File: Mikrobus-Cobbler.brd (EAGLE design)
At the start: 54.6 x 36.8 mm, 2 parts

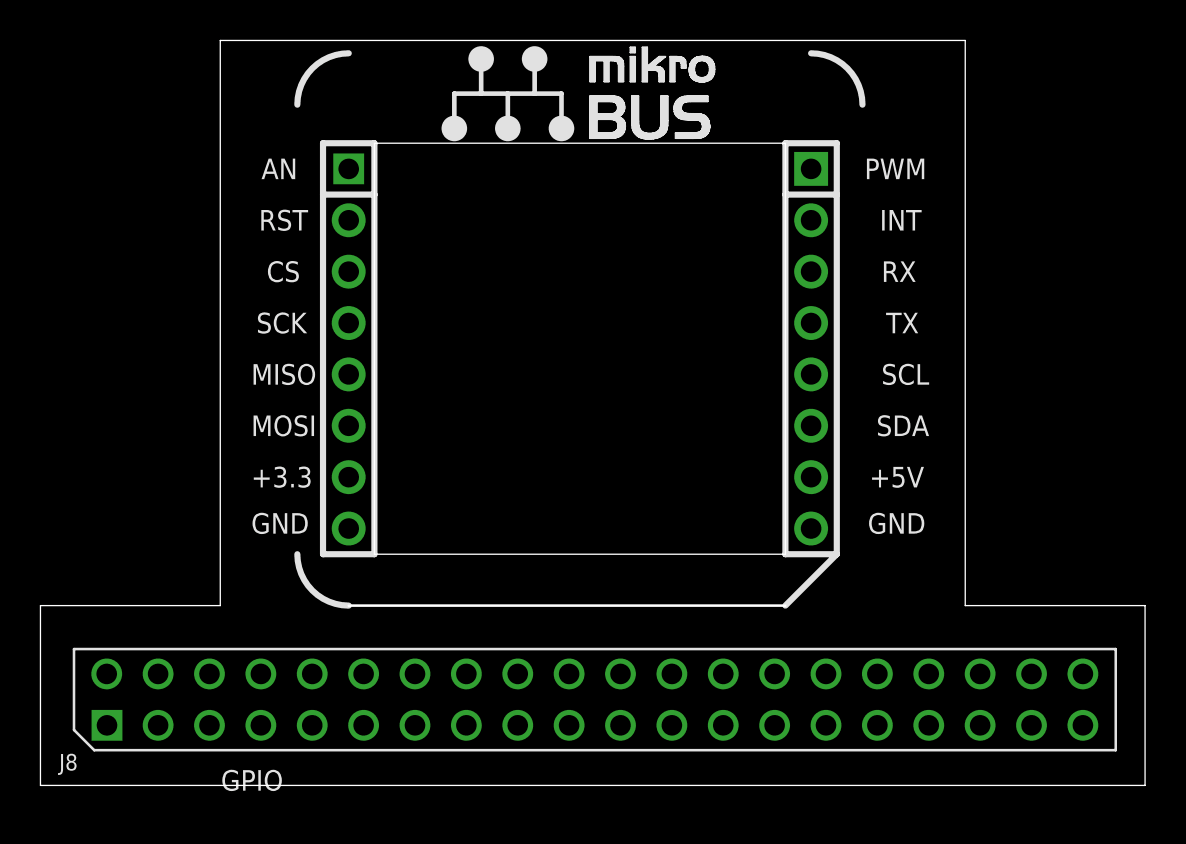
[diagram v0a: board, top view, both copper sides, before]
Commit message: rotated part this makes it easier for routing, ground plane on top
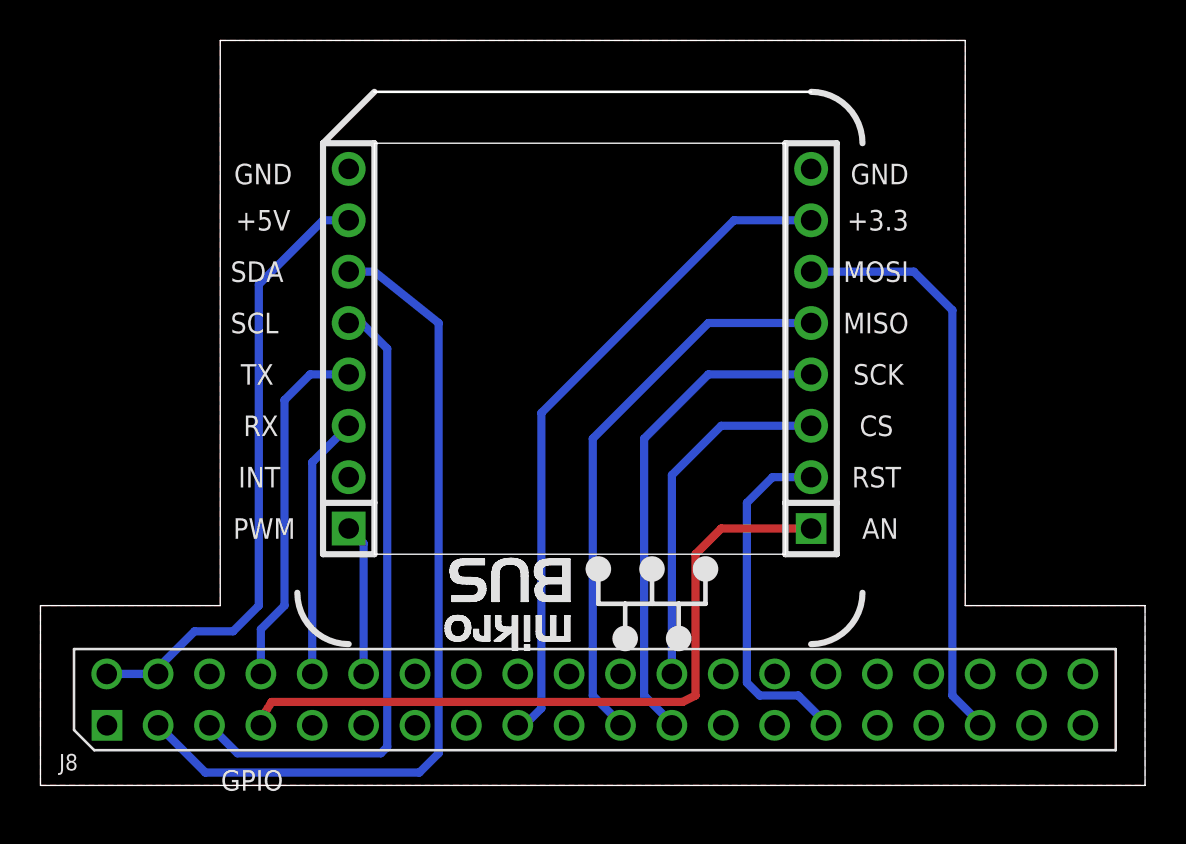
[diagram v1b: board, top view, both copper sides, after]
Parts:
- moved MB1 2.54 mm to (26.7, 20.3), turned to 180 degrees
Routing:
- net N$15: track 0.00 -> 41.8 mm
- net N$4: track 0.00 -> 35.6 mm
- net N$3: track 0.00 -> 33.4 mm
- net N$14: track 0.00 -> 31.6 mm
- net N$2: track 0.00 -> 30.7 mm
- net N$9: track 0.00 -> 28.9 mm
- net N$8: track 0.00 -> 28.0 mm
- net N$6: track 0.00 -> 24.3 mm
- net N$7: track 0.00 -> 17.7 mm
- net N$13: track 0.00 -> 17.7 mm
- net N$5: track 0.00 -> 17.4 mm
- net N$12: track 0.00 -> 13.0 mm
- net N$10: track 0.00 -> 7.49 mm
- added copper zone on layer 1, net N$1

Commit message: Put back board and roughly routed
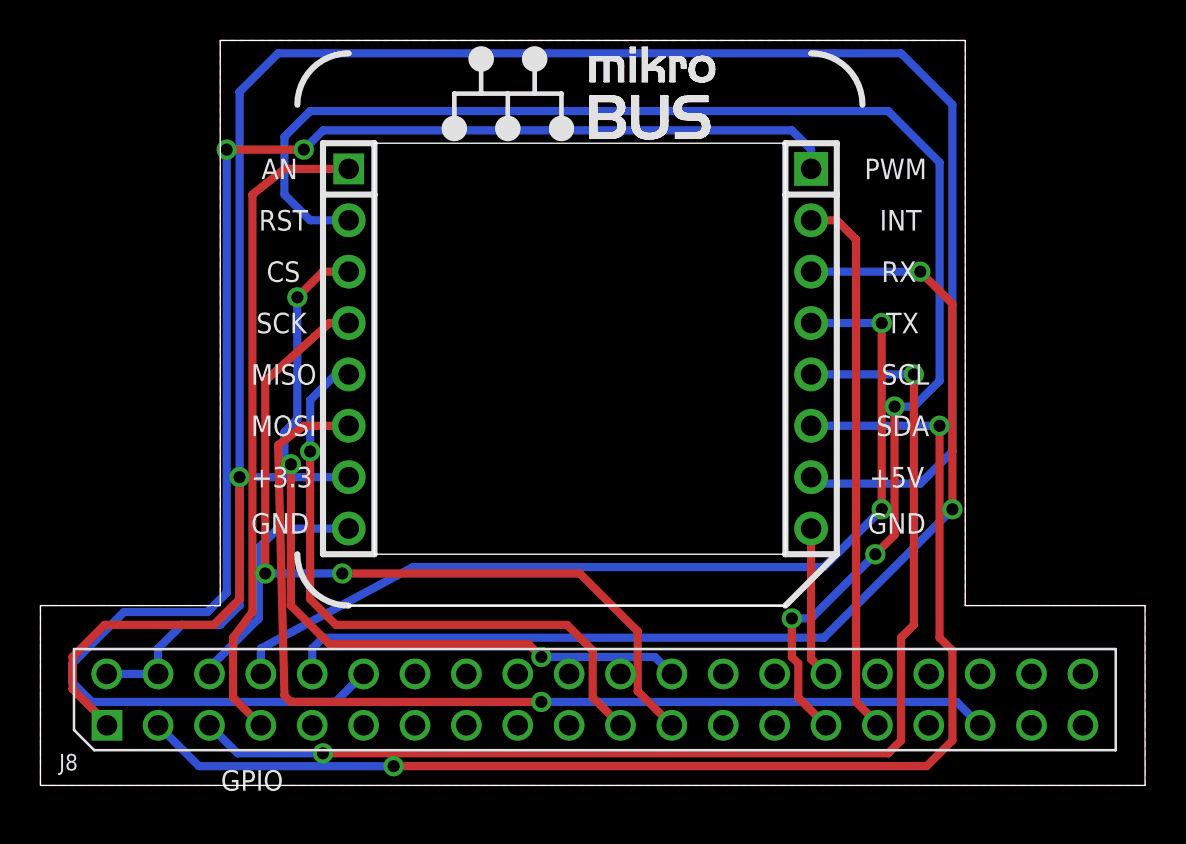
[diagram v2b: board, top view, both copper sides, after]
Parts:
- moved MB1 2.54 mm to (26.7, 22.9), turned to 0 degrees
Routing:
- net N$10: track 7.49 -> 77.9 mm, vias 0 -> 2
- net N$2: track 30.7 -> 96.1 mm
- net N$5: track 17.4 -> 73.2 mm, vias 0 -> 3
- net N$12: track 13.0 -> 53.6 mm, vias 0 -> 2
- net N$13: track 17.7 -> 46.8 mm, vias 0 -> 2
- net N$11: track 0.00 -> 27.1 mm
- net N$14: track 31.6 -> 58.5 mm, vias 0 -> 2
- net N$9: track 28.9 -> 51.2 mm, vias 0 -> 1
- net N$7: track 17.7 -> 38.9 mm, vias 0 -> 3
- net N$15: track 41.8 -> 62.8 mm, vias 0 -> 2
- net N$1: track 0.00 -> 19.6 mm
- net N$6: track 24.3 -> 39.7 mm, vias 0 -> 2
- net N$3: track 33.4 -> 25.0 mm, vias 0 -> 1
- net N$8: track 28.0 -> 31.6 mm, vias 0 -> 1
- net N$4: track 35.6 -> 32.3 mm
